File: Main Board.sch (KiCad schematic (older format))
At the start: 12 parts

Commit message: Update elements value
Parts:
- FID1, FID2, FID3, FID4, FID5, FID6, H1, H2, H3, H4, H5, H6: Cena (none) -> 0
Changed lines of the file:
@@
 F 2 "MountingHole:MountingHole_3.5mm_Pad_Via" H 8600 2100 50  0001 C CNN
 F 3 "~" H 8600 2100 50  0001 C CNN
+F 4 "0" H 8600 2100 50  0001 C CNN "Cena"
 	1    8600 2100
 	1    0    0    -1
@@
 F 2 "MountingHole:MountingHole_3.5mm_Pad_Via" H 8900 2100 50  0001 C CNN
 F 3 "~" H 8900 2100 50  0001 C CNN
+F 4 "0" H 8900 2100 50  0001 C CNN "Cena"
 	1    8900 2100
 	1    0    0    -1
@@
 F 2 "MountingHole:MountingHole_3.5mm_Pad_Via" H 9200 2100 50  0001 C CNN
 F 3 "~" H 9200 2100 50  0001 C CNN
+F 4 "0" H 9200 2100 50  0001 C CNN "Cena"
 	1    9200 2100
 	1    0    0    -1
@@
 F 2 "MountingHole:MountingHole_3.5mm_Pad_Via" H 9500 2100 50  0001 C CNN
 F 3 "~" H 9500 2100 50  0001 C CNN
+F 4 "0" H 9500 2100 50  0001 C CNN "Cena"
 	1    9500 2100
 	1    0    0    -1
@@
 F 2 "MountingHole:MountingHole_3.5mm_Pad_Via" H 9800 2100 50  0001 C CNN
 F 3 "~" H 9800 2100 50  0001 C CNN
+F 4 "0" H 9800 2100 50  0001 C CNN "Cena"
 	1    9800 2100
 	1    0    0    -1
@@
 F 2 "MountingHole:MountingHole_3.5mm_Pad_Via" H 10100 2100 50  0001 C CNN
 F 3 "~" H 10100 2100 50  0001 C CNN
+F 4 "0" H 10100 2100 50  0001 C CNN "Cena"
 	1    10100 2100
 	1    0    0    -1
@@
 F 2 "Fiducial:Fiducial_1mm_Mask2mm" H 8650 3050 50  0001 C CNN
 F 3 "~" H 8650 3050 50  0001 C CNN
+F 4 "0" H 8650 3050 50  0001 C CNN "Cena"
 	1    8650 3050
 	1    0    0    -1
@@
 F 2 "Fiducial:Fiducial_1mm_Mask2mm" H 9150 3050 50  0001 C CNN
 F 3 "~" H 9150 3050 50  0001 C CNN
+F 4 "0" H 9150 3050 50  0001 C CNN "Cena"
 	1    9150 3050
 	1    0    0    -1
@@
 F 2 "Fiducial:Fiducial_1mm_Mask2mm" H 9650 3050 50  0001 C CNN
 F 3 "~" H 9650 3050 50  0001 C CNN
+F 4 "0" H 9650 3050 50  0001 C CNN "Cena"
 	1    9650 3050
 	1    0    0    -1
@@
 F 2 "Fiducial:Fiducial_1mm_Mask2mm" H 10150 3050 50  0001 C CNN
 F 3 "~" H 10150 3050 50  0001 C CNN
+F 4 "0" H 10150 3050 50  0001 C CNN "Cena"
 	1    10150 3050
 	1    0    0    -1
@@
 F 2 "Fiducial:Fiducial_1mm_Mask2mm" H 8650 3300 50  0001 C CNN
 F 3 "~" H 8650 3300 50  0001 C CNN
+F 4 "0" H 8650 3300 50  0001 C CNN "Cena"
 	1    8650 3300
 	1    0    0    -1
@@
 F 2 "Fiducial:Fiducial_1mm_Mask2mm" H 9150 3300 50  0001 C CNN
 F 3 "~" H 9150 3300 50  0001 C CNN
+F 4 "0" H 9150 3300 50  0001 C CNN "Cena"
 	1    9150 3300
 	1    0    0    -1

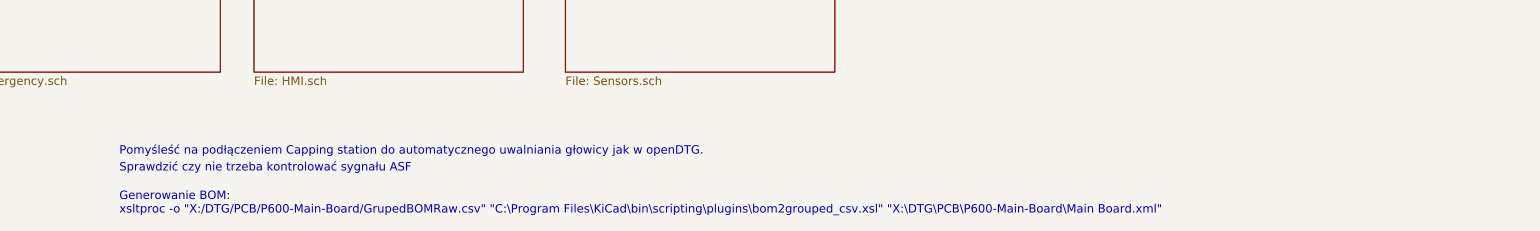
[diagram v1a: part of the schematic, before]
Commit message: Updated BOM on schematics
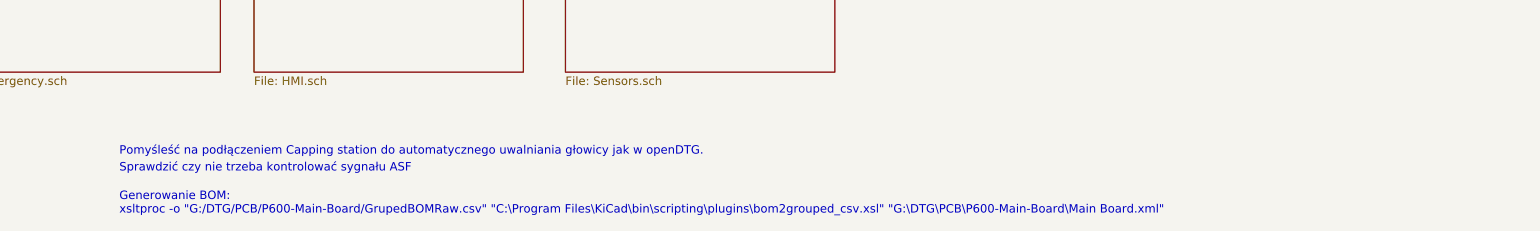
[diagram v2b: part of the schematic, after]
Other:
- note added: "Generowanie BOM:\nxsltproc -o "G:/DTG/PCB/P600-Main-Board/GrupedBOMRaw.csv" "C:\Program Files\KiCad\bin\scripting\plugins\bom2grouped_csv.xsl" "G:\DTG\PCB\P600-Main-Board\Main Board.xml""
- note removed: "Generowanie BOM:\nxsltproc -o "X:/DTG/PCB/P600-Main-Board/GrupedBOMRaw.csv" "C:\Program Files\KiCad\bin\scripting\plugins\bom2grouped_csv.xsl" "X:\DTG\PCB\P600-Main-Board\Main Board.xml""
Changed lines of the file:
@@
 Fiducials
 Text Notes 2750 5000 0    50   ~ 0
-Generowanie BOM:\nxsltproc -o "X:/DTG/PCB/P600-Main-Board/GrupedBOMRaw.csv" "C:\Program Files\KiCad\bin\scripting\plugins\bom2grouped_csv.xsl" "X:\DTG\PCB\P600-Main-Board\Main Board.xml"
+Generowanie BOM:\nxsltproc -o "G:/DTG/PCB/P600-Main-Board/GrupedBOMRaw.csv" "C:\Program Files\KiCad\bin\scripting\plugins\bom2grouped_csv.xsl" "G:\DTG\PCB\P600-Main-Board\Main Board.xml"
 $Comp
 L Mechanical:Fiducial FID5
